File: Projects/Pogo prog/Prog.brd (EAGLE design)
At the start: 17.8 x 12.7 mm, 1 part, among them J1 RA 6Pin SMD

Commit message: Final design
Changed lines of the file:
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@@
 <via x="6.35" y="46.99" extent="1-16" drill="1.3"/>
 <contactref element="J1" pad="6"/>
-<via x="6.35" y="53.34" extent="1-16" drill="0.4"/>
-<via x="6.35" y="52.07" extent="1-16" drill="0.4"/>
-<via x="6.35" y="50.8" extent="1-16" drill="0.4"/>
+<via x="6.35" y="53.34" extent="1-16" drill="0.5"/>
+<via x="6.35" y="52.07" extent="1-16" drill="0.5"/>
+<via x="6.35" y="50.8" extent="1-16" drill="0.5"/>
 <wire x1="6.35" y1="50.8" x2="6.35" y2="46.99" width="0.508" layer="1"/>
 <wire x1="6.35" y1="52.15" x2="6.35" y2="53.34" width="0" layer="19" extent="1-1"/>
@@
 <via x="8.89" y="45.72" extent="1-16" drill="1.3"/>
 <contactref element="J1" pad="5"/>
-<via x="8.89" y="50.8" extent="1-16" drill="0.4"/>
-<via x="8.89" y="52.07" extent="1-16" drill="0.4"/>
-<via x="8.89" y="53.34" extent="1-16" drill="0.4"/>
+<via x="8.89" y="50.8" extent="1-16" drill="0.5"/>
+<via x="8.89" y="52.07" extent="1-16" drill="0.5"/>
+<via x="8.89" y="53.34" extent="1-16" drill="0.5"/>
 <wire x1="8.89" y1="45.72" x2="8.89" y2="52.07" width="0.508" layer="1"/>
 <wire x1="8.89" y1="52.15" x2="8.89" y2="53.34" width="0" layer="19" extent="1-1"/>
@@
 <via x="13.97" y="45.72" extent="1-16" drill="1.3"/>
 <contactref element="J1" pad="3"/>
-<via x="13.97" y="53.34" extent="1-16" drill="0.4"/>
-<via x="13.97" y="52.07" extent="1-16" drill="0.4"/>
-<via x="13.97" y="50.8" extent="1-16" drill="0.4"/>
+<via x="13.97" y="53.34" extent="1-16" drill="0.5"/>
+<via x="13.97" y="52.07" extent="1-16" drill="0.5"/>
+<via x="13.97" y="50.8" extent="1-16" drill="0.5"/>
 <wire x1="13.97" y1="45.72" x2="13.97" y2="52.15" width="0.508" layer="1"/>
 <wire x1="13.97" y1="52.15" x2="13.97" y2="53.34" width="0" layer="19" extent="1-1"/>
@@
 <contactref element="J1" pad="4"/>
 <via x="11.43" y="46.99" extent="1-16" drill="1.3"/>
-<via x="11.43" y="53.34" extent="1-16" drill="0.4"/>
-<via x="11.43" y="52.07" extent="1-16" drill="0.4"/>
-<via x="11.43" y="50.8" extent="1-16" drill="0.4"/>
+<via x="11.43" y="53.34" extent="1-16" drill="0.5"/>
+<via x="11.43" y="52.07" extent="1-16" drill="0.5"/>
+<via x="11.43" y="50.8" extent="1-16" drill="0.5"/>
 <wire x1="11.43" y1="46.99" x2="11.43" y2="52.15" width="0.508" layer="1"/>
 <wire x1="11.43" y1="52.15" x2="11.43" y2="53.34" width="0" layer="19" extent="1-1"/>
@@
 </signal>
 <signal name="N$15">
-<via x="16.51" y="53.34" extent="1-16" drill="0.4"/>
+<via x="16.51" y="53.34" extent="1-16" drill="0.5"/>
 </signal>
 <signal name="N$16">
-<via x="16.51" y="52.07" extent="1-16" drill="0.4"/>
+<via x="16.51" y="52.07" extent="1-16" drill="0.5"/>
 </signal>
 <signal name="N$17">
-<via x="16.51" y="50.8" extent="1-16" drill="0.4"/>
+<via x="16.51" y="50.8" extent="1-16" drill="0.5"/>
 </signal>
 <signal name="N$18">
-<via x="19.05" y="53.34" extent="1-16" drill="0.4"/>
+<via x="19.05" y="53.34" extent="1-16" drill="0.5"/>
 </signal>
 <signal name="N$19">
-<via x="19.05" y="52.07" extent="1-16" drill="0.4"/>
+<via x="19.05" y="52.07" extent="1-16" drill="0.5"/>
 </signal>
 <signal name="N$20">
-<via x="19.05" y="50.8" extent="1-16" drill="0.4"/>
+<via x="19.05" y="50.8" extent="1-16" drill="0.5"/>
 </signal>
 </signals>

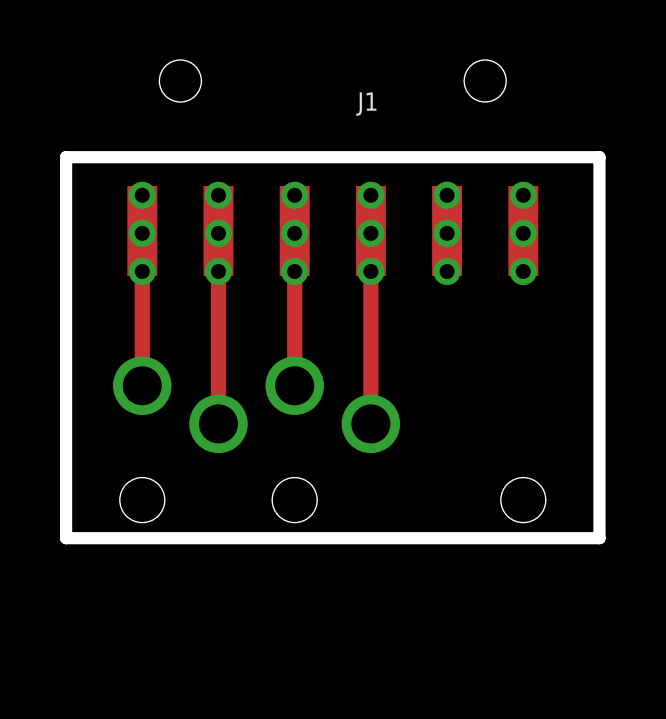
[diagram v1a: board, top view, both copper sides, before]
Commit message: Added one more pogo pin
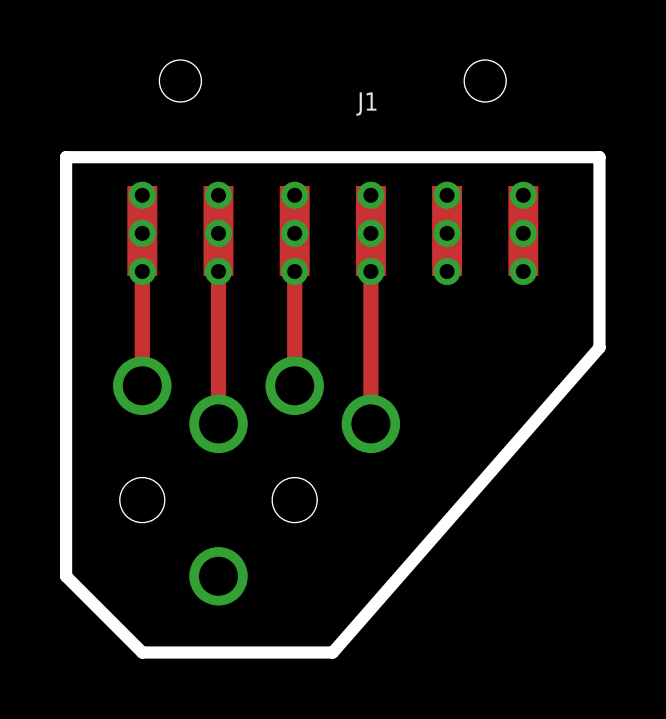
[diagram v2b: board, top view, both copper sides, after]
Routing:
- net PIN2: vias 4 -> 5
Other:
- board size 17.8 x 12.7 mm -> 17.8 x 16.5 mm
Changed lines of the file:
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@@
 <?xml version="1.0" encoding="utf-8"?>
 <!DOCTYPE eagle SYSTEM "eagle.dtd">
-<eagle version="8.4.0">
+<eagle version="9.0.1">
 <drawing>
 <settings>
@@
 <hole x="11.43" y="43.18" drill="1.5"/>
 <wire x1="3.81" y1="54.61" x2="21.59" y2="54.61" width="0.4064" layer="20"/>
-<wire x1="21.59" y1="54.61" x2="21.59" y2="41.91" width="0.4064" layer="20"/>
-<wire x1="21.59" y1="41.91" x2="3.81" y2="41.91" width="0.4064" layer="20"/>
-<wire x1="3.81" y1="41.91" x2="3.81" y2="54.61" width="0.4064" layer="20"/>
+<wire x1="21.59" y1="54.61" x2="21.59" y2="48.26" width="0.4064" layer="20"/>
+<wire x1="21.59" y1="48.26" x2="12.7" y2="38.1" width="0.4064" layer="20"/>
+<wire x1="12.7" y1="38.1" x2="6.35" y2="38.1" width="0.4064" layer="20"/>
+<wire x1="6.35" y1="38.1" x2="3.81" y2="40.64" width="0.4064" layer="20"/>
+<wire x1="3.81" y1="40.64" x2="3.81" y2="54.61" width="0.4064" layer="20"/>
 <hole x="6.35" y="43.18" drill="1.5"/>
-<hole x="19.05" y="43.18" drill="1.5"/>
 </plain>
 <attributes>
@@
 <param name="dpMaxLengthDifference" value="10mm"/>
 <param name="dpGapFactor" value="2.5"/>
+<param name="checkAngle" value="0"/>
 <param name="checkFont" value="1"/>
 <param name="checkRestrict" value="1"/>
 <param name="checkStop" value="0"/>
+<param name="checkValues" value="0"/>
 <param name="useDiameter" value="13"/>
 <param name="maxErrors" value="50"/>
@@
 <wire x1="8.89" y1="52.07" x2="8.89" y2="52.15" width="0" layer="19" extent="1-1"/>
 <wire x1="8.89" y1="50.8" x2="8.89" y2="52.07" width="0" layer="19" extent="1-1"/>
+<via x="8.89" y="40.64" extent="1-16" drill="1.3"/>
 </signal>
 <signal name="GND">

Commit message: Corrected mistakes on myStravaV10
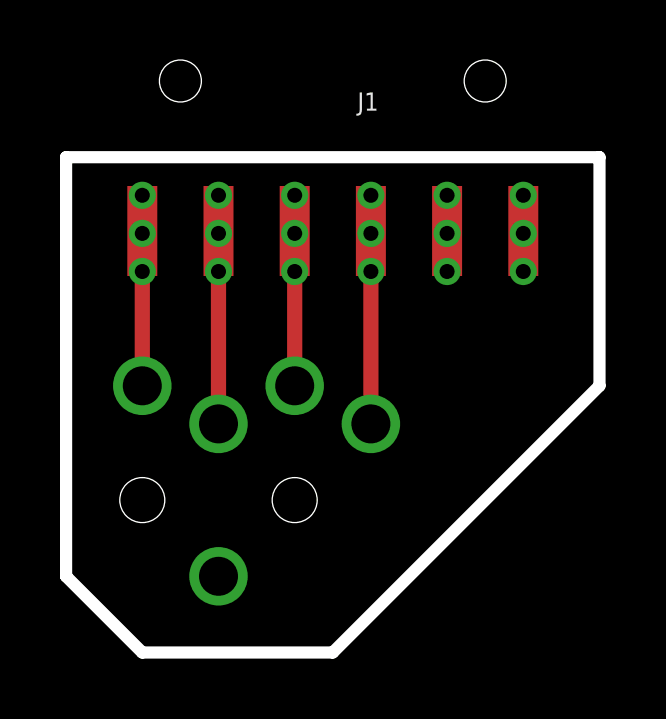
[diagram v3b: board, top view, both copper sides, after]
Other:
- outline, holes or cut-outs redrawn
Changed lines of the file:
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@@
 <hole x="11.43" y="43.18" drill="1.5"/>
 <wire x1="3.81" y1="54.61" x2="21.59" y2="54.61" width="0.4064" layer="20"/>
-<wire x1="21.59" y1="54.61" x2="21.59" y2="48.26" width="0.4064" layer="20"/>
-<wire x1="21.59" y1="48.26" x2="12.7" y2="38.1" width="0.4064" layer="20"/>
+<wire x1="21.59" y1="54.61" x2="21.59" y2="46.99" width="0.4064" layer="20"/>
+<wire x1="21.59" y1="46.99" x2="12.7" y2="38.1" width="0.4064" layer="20"/>
 <wire x1="12.7" y1="38.1" x2="6.35" y2="38.1" width="0.4064" layer="20"/>
 <wire x1="6.35" y1="38.1" x2="3.81" y2="40.64" width="0.4064" layer="20"/>
@@
 <via x="8.89" y="53.34" extent="1-16" drill="0.5"/>
 <wire x1="8.89" y1="45.72" x2="8.89" y2="52.07" width="0.508" layer="1"/>
+<via x="8.89" y="40.64" extent="1-16" drill="1.3"/>
 <wire x1="8.89" y1="52.15" x2="8.89" y2="53.34" width="0" layer="19" extent="1-1"/>
 <wire x1="8.89" y1="52.07" x2="8.89" y2="52.15" width="0" layer="19" extent="1-1"/>
 <wire x1="8.89" y1="50.8" x2="8.89" y2="52.07" width="0" layer="19" extent="1-1"/>
-<via x="8.89" y="40.64" extent="1-16" drill="1.3"/>
+<wire x1="8.89" y1="40.64" x2="8.89" y2="45.72" width="0" layer="19" extent="1-1"/>
 </signal>
 <signal name="GND">
